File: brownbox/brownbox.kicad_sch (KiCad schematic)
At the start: 341 parts, among them J1 Rifle Connector - C7-205, J2 12-Pin Cinch Jones Expansion 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, J3 Jumper, Q1 2N5134, Q10 2N5134, Q11 2N5133, Q12 2N5134, Q13 2N5134, Q14 2N5134, Q15 2N5133, Q16 2N5134, Q17 2N5134, Q18 2N5134, Q19 2N5133, Q2 2N5139, Q20 2N5134, Q21 2N5133, Q22 2N5139, Q23 2N5133, Q24 2N5139, Q25 2N5133, Q26 2N5139, Q27 2N5133, Q28 2N5139, Q29 2N5134, Q3 2N5134, Q30 2N5134, Q31 2N5133, Q32 2N5133, Q33 2N5133, Q34 2N5133, Q35 2N5134, Q36 2N5134, Q37 2N5133, Q38 2N5133, Q39 2N5133, Q4 2N5139, Q40 2N5139, Q41 2N5139, Q42 2N5133, Q43 2N5139, Q44 2N5133, Q45 2N5133, Q46 2N5133, Q5 2N5134, Q6 2N5134, Q7 2N5133, Q8 2N5134, Q9 2N5134, T1 CF104 core, #22 wire, X1 3.579545Mhz

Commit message: Update BJTs with TO-92/TO-106 compatible footprints
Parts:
- Q1, Q10, Q11, Q12, Q13, Q14, Q15, Q16, Q17, Q18, Q19, Q2, Q20, Q21, Q22, Q23, Q24, Q25, Q26, Q27, Q28, Q29, Q3, Q30, Q31, Q32, Q33, Q34, Q35, Q36, Q37, Q38, Q39, Q4, Q40, Q41, Q42, Q43, Q44, Q45, Q46, Q5, Q6, Q7, Q8, Q9: footprint Package_TO_SOT_THT:TO-92_Inline -> footprints:TO-92_Offset_TO-106

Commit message: capacitor footprints picked and some layout started
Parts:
- C1, C10, C11, C12, C13, C14, C15, C16, C17, C18, C19, C2, C20, C21, C22, C23, C24, C25, C26, C27, C28, C29, C3, C30, C31, C32, C33, C34, C35, C36, C37, C38, C39, C4, C40, C41, C42, C43, C44, C45, C46, C47, C48, C49, C5, C50, C51, C52, C53, C54, C55, C56, C6, C7, C8, C9, CV1, CV2: footprint (none) -> Capacitor_THT:C_Disc_D5.0mm_W2.5mm_P5.00mm

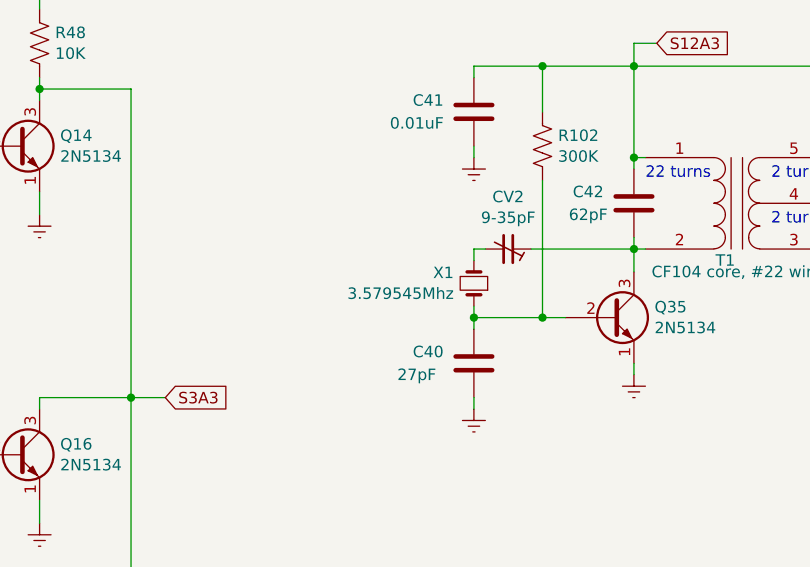
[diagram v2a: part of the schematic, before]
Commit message: finished initial placement
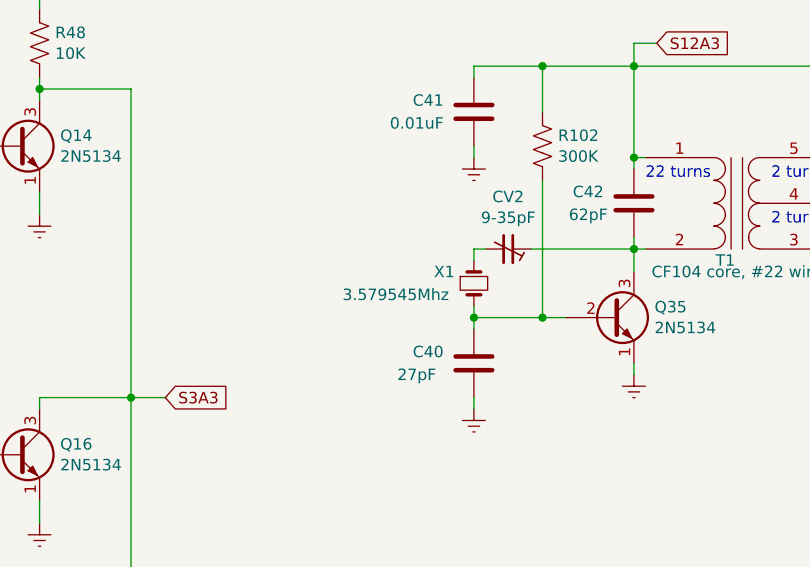
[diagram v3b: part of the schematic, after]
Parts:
- X1: footprint (none) -> Crystal:Crystal_HC49-U_Horizontal
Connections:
- net at C40.2, Q35.2 (B), R102.2: now also X1.2; no longer X1.1
- net at CV2.2: now also X1.1; no longer X1.2
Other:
- moved on the sheet: X1
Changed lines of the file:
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@@
     (pin "2")
   )
-  (symbol (lib_id "Device:Crystal_Small") (at 393.7 67.31 90) (unit 1)
-    (in_bom yes) (on_board yes)
-    (property "Reference" "X1" (id 0) (at 391.4648 66.1416 90)
-      (effects (font (size 1.27 1.27)) (justify left))
-    )
-    (property "Value" "3.579545Mhz" (id 1) (at 391.4648 68.453 90)
-      (effects (font (size 1.27 1.27)) (justify left))
-    )
-    (property "Footprint" "" (id 2) (at 393.7 67.31 0)
+  (symbol (lib_id "Device:Crystal_Small") (at 393.7 67.31 270) (unit 1)
+    (in_bom yes) (on_board yes)
+    (property "Reference" "X1" (id 0) (at 389.255 66.04 90)
+      (effects (font (size 1.27 1.27)) (justify left))
+    )
+    (property "Value" "3.579545Mhz" (id 1) (at 379.095 68.58 90)
+      (effects (font (size 1.27 1.27)) (justify left))
+    )
+    (property "Footprint" "Crystal:Crystal_HC49-U_Horizontal" (id 2) (at 393.7 67.31 0)
       (effects (font (size 1.27 1.27)) hide)
     )
@@
     )
     (path "/00000000-0000-0000-0000-00006d86c760"
-      (reference "X1") (unit 1) (value "3.579545Mhz") (footprint "")
-    )
-  )
+      (reference "X1") (unit 1) (value "3.579545Mhz") (footprint "Crystal:Crystal_HC49-U_Horizontal")
+    )
+  )

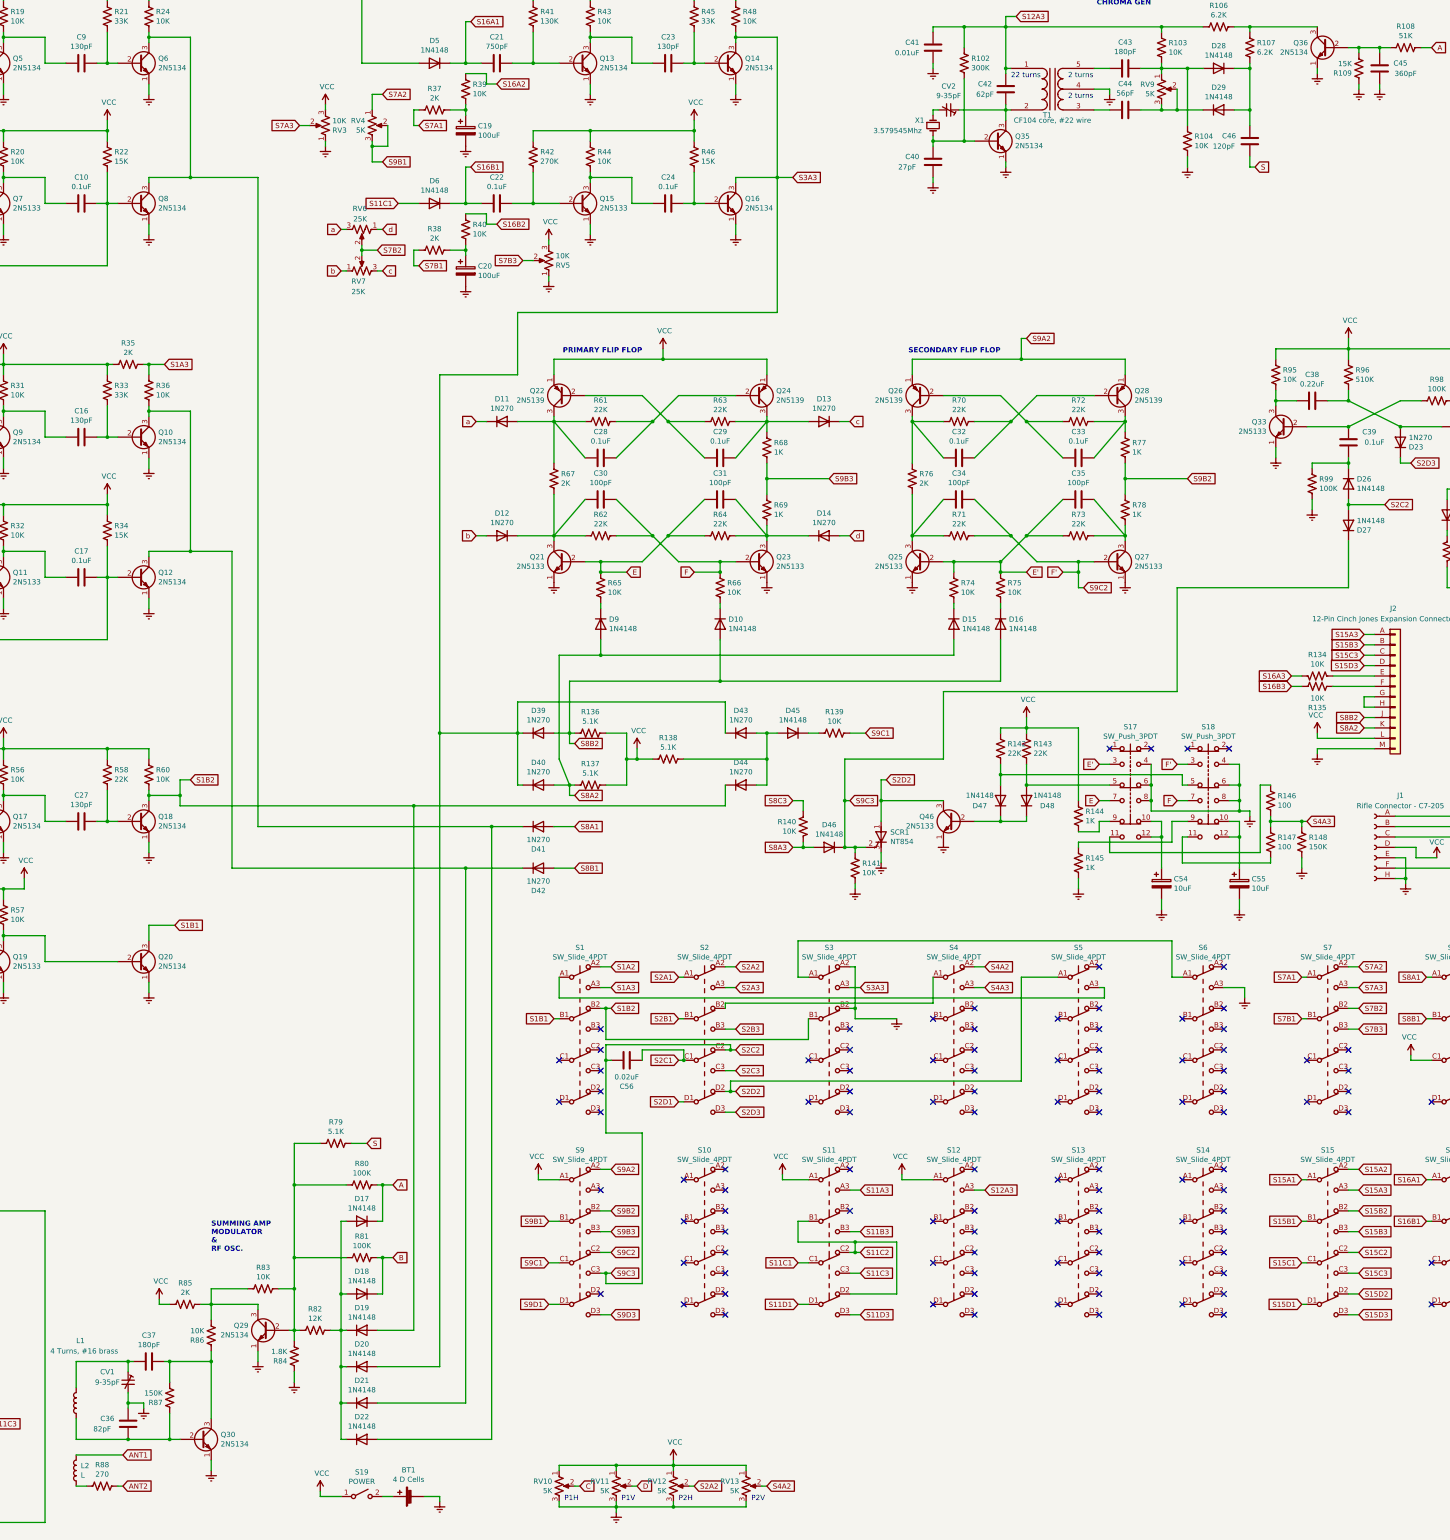
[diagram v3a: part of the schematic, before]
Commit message: routed board without buttons
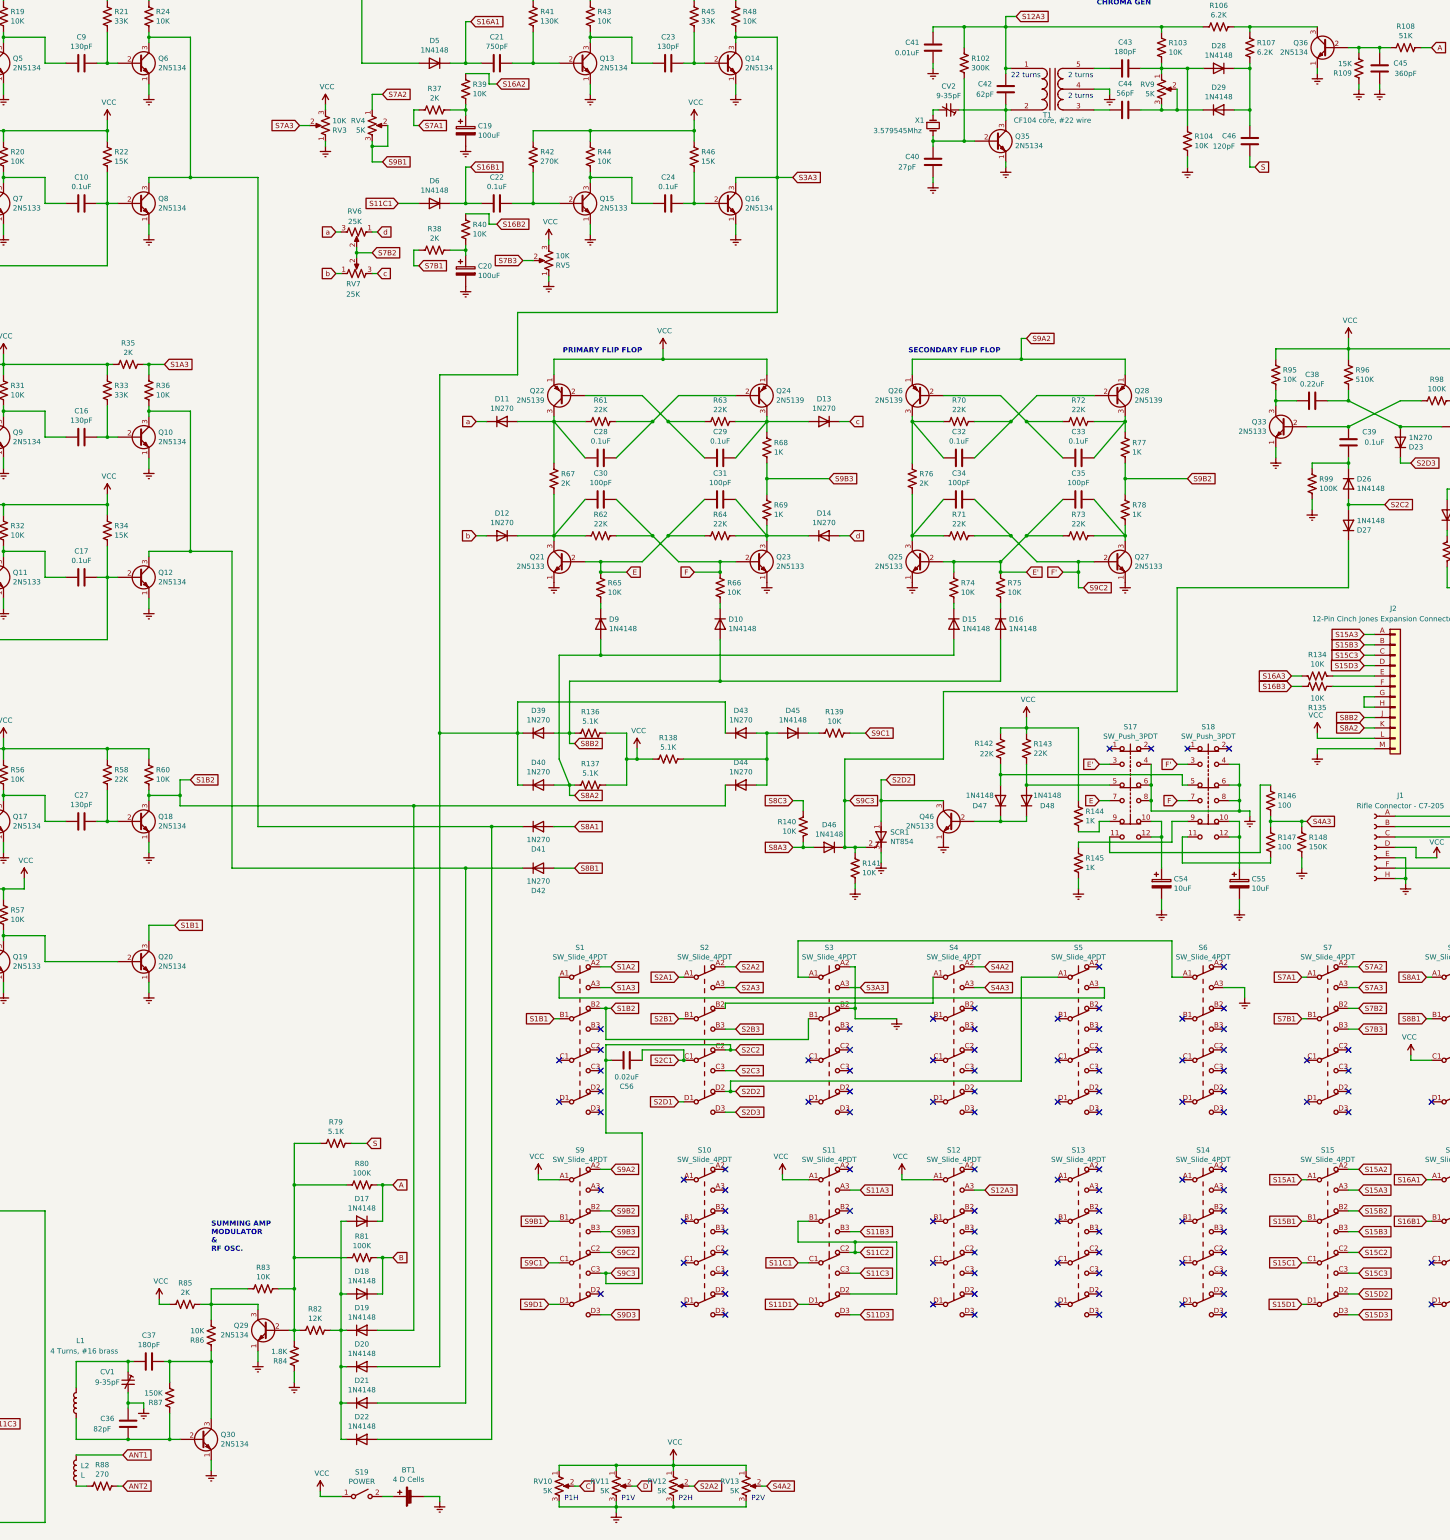
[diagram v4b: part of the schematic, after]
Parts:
- L1, L2: footprint (none) -> Inductor_THT:L_Axial_L5.3mm_D2.2mm_P7.62mm_Horizontal_Vishay_IM-1
- S1, S10, S11, S12, S13, S14, S15, S16, S2, S3, S4, S5, S6, S7, S8, S9: footprint (none) -> Evan's parts:MFS401N2Z_brownbox
- S19: footprint (none) -> Connector_PinHeader_2.54mm:PinHeader_2x01_P2.54mm_Vertical
- T1: footprint (none) -> Evan's parts:brownbox_transformer
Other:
- moved on the sheet: RV6, RV7

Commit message: finished layout
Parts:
- S17, S18: footprint (none) -> Evan's parts:honeywell 3pdt switch
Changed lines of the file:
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@@
       (effects (font (size 1.27 1.27)))
     )
-    (property "Footprint" "" (at 441.96 216.535 0)
+    (property "Footprint" "Evan's parts:honeywell 3pdt switch" (at 441.96 216.535 0)
       (effects (font (size 1.27 1.27)) hide)
     )
@@
       (effects (font (size 1.27 1.27)))
     )
-    (property "Footprint" "" (at 461.01 216.535 0)
+    (property "Footprint" "Evan's parts:honeywell 3pdt switch" (at 461.01 216.535 0)
       (effects (font (size 1.27 1.27)) hide)
     )

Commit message: updated pcb for fab
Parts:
- added TP1: ANT1, Connector_PinHeader_2.54mm:PinHeader_1x01_P2.54mm_Vertical, symbol Connector:TestPoint
- added TP2: ANT2, Connector_PinHeader_2.54mm:PinHeader_1x01_P2.54mm_Vertical, symbol Connector:TestPoint
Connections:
- net ANT1: no longer names the net of L2.2
- net ANT1: now also TP1.1
- net ANT2: no longer names the net of R88.2
- net ANT2: now also TP2.1
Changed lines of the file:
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@@
     )
   )
-  (global_label "ANT2" (shape input) (at 195.58 400.05 0) (fields_autoplaced)
-    (effects (font (size 1.27 1.27)) (justify left))
-    (property "Intersheetrefs" "${INTERSHEET_REFS}" (at 202.4278 400.05 0)
-      (effects (font (size 1.27 1.27)) (justify left) hide)
-    )
-  )
   (global_label "c" (shape input) (at 373.38 139.7 0) (fields_autoplaced)
     (effects (font (size 1.27 1.27)) (justify left))
@@
     )
   )
-  (global_label "ANT1" (shape input) (at 195.58 392.43 0) (fields_autoplaced)
-    (effects (font (size 1.27 1.27)) (justify left))
-    (property "Intersheetrefs" "${INTERSHEET_REFS}" (at 202.4278 392.43 0)
-      (effects (font (size 1.27 1.27)) (justify left) hide)
-    )
-  )
   (global_label "A" (shape input) (at 261.62 326.39 0) (fields_autoplaced)
     (effects (font (size 1.27 1.27)) (justify left))
@@
         )
       )
+    )
+  )
+  (symbol (lib_id "Connector:TestPoint") (at 195.58 400.05 270) (unit 1)
+    (in_bom yes) (on_board yes) (dnp no) (fields_autoplaced)
+    (property "Reference" "TP2" (at 200.279 399.4063 90)
+      (effects (font (size 1.27 1.27)) (justify left))
+    )
+    (property "Value" "ANT2" (at 200.279 401.3273 90)
+      (effects (font (size 1.27 1.27)) (justify left))
+    )
+    (property "Footprint" "Connector_PinHeader_2.54mm:PinHeader_1x01_P2.54mm_Vertical" (at 195.58 405.13 0)
+      (effects (font (size 1.27 1.27)) hide)
+    )
+    (property "Datasheet" "~" (at 195.58 405.13 0)
+      (effects (font (size 1.27 1.27)) hide)
+    )
+    (pin "1")
+    (instances
+      (project "brownbox"
+        (path "/1f8b2c0c-b042-4e2e-80f6-4959a27b238f"
+          (reference "TP2") (unit 1)
+        )
+      )
+    )
+  )
+  (symbol (lib_id "Connector:TestPoint") (at 195.58 392.43 270) (unit 1)
+    (in_bom yes) (on_board yes) (dnp no) (fields_autoplaced)
+    (property "Reference" "TP1" (at 200.279 391.7863 90)
+      (effects (font (size 1.27 1.27)) (justify left))
+    )
+    (property "Value" "ANT1" (at 200.279 393.7073 90)
+      (effects (font (size 1.27 1.27)) (justify left))
+    )
+    (property "Footprint" "Connector_PinHeader_2.54mm:PinHeader_1x01_P2.54mm_Vertical" (at 195.58 397.51 0)
+      (effects (font (size 1.27 1.27)) hide)
+    )
+    (property "Datasheet" "~" (at 195.58 397.51 0)
+      (effects (font (size 1.27 1.27)) hide)
+    )
+    (pin "1")
+    (instances
+      (project "brownbox"
+        (path "/1f8b2c0c-b042-4e2e-80f6-4959a27b238f"
+          (reference "TP1") (unit 1)
+        )
+      )
